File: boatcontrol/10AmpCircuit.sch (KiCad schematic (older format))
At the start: 5 parts, among them K6801 G5RL-K1A-E-DC12, Q6801 T9-818 10A, SW6801 ESB30, SW6802 ESB30

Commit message: Fix graphics
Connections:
- net ON_COIL: now reaches K6801.1 (C1), SW6801.2 (B), SW6801.5 (B)
- net TO_FUSE: now reaches K6801.4 (NO), K6801.5 (NO), Q6801.P1 (P?)
- net OFF_COIL: now reaches K6801.8 (C8), SW6802.2 (B), SW6802.5 (B)
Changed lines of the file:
@@
 $Descr A4 11693 8268
 encoding utf-8
-Sheet 67 87
+Sheet 76 87
 Title "Boat Control Hat"
 Date "2020-07-09"
@@
 Wire Wire Line
 	5250 4000 5250 4900
+Text Label 6750 3550 0    50   ~ 0
+ON_COIL
+Text Label 6700 4500 0    50   ~ 0
+OFF_COIL
+Text Label 7350 3650 0    50   ~ 0
+TO_FUSE
 $EndSCHEMATC

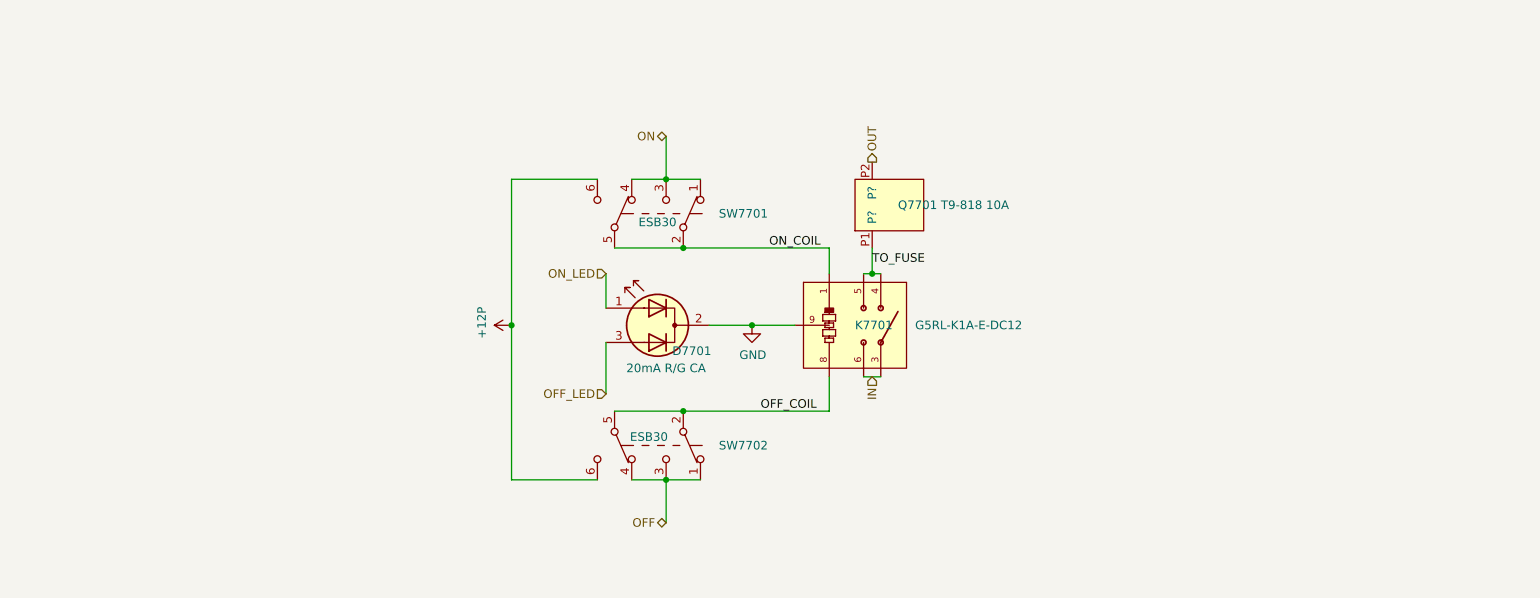
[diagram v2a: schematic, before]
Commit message: Fix switch layouts
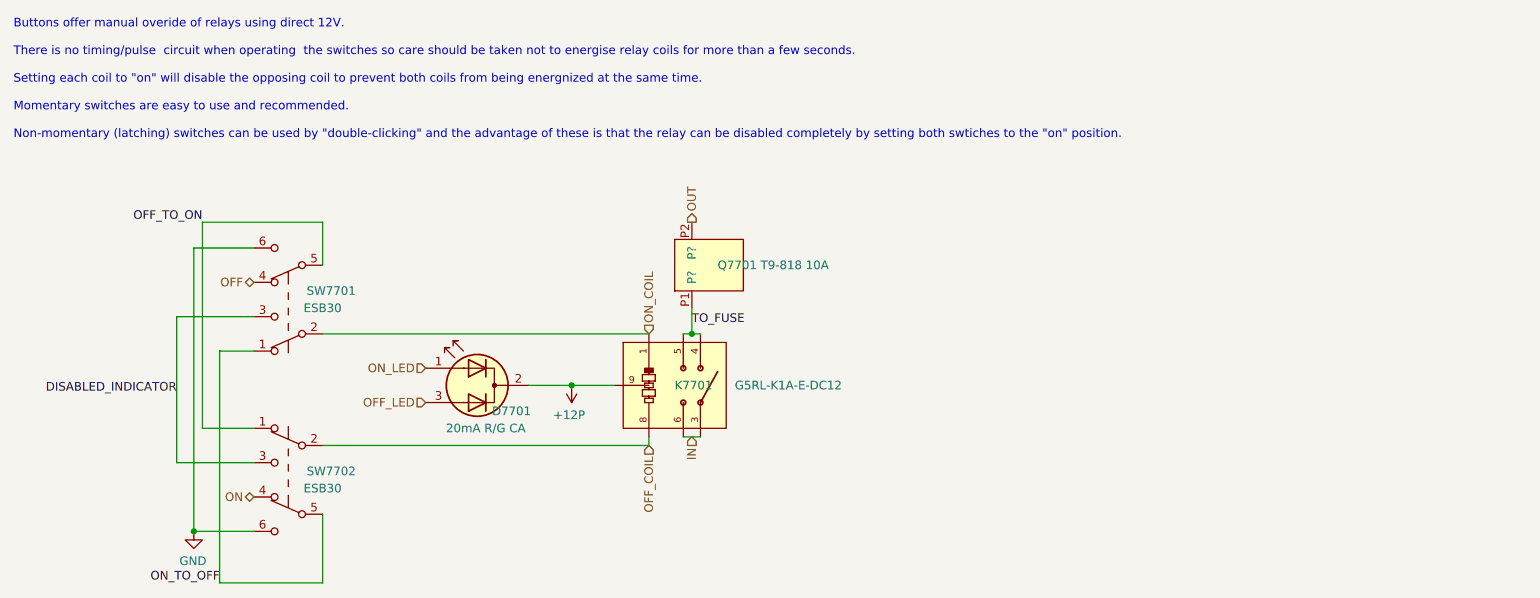
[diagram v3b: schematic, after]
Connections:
- net +12P: now also D6801.2 (K), K6801.9 (C9); no longer SW6801.6 (C), SW6802.6 (C)
- net GND: now also SW6801.6 (C), SW6802.6 (C); no longer D6801.2 (K), K6801.9 (C9)
- net OFF: now also SW6801.4 (A); no longer SW6802.1 (A), SW6802.3 (C), SW6802.4 (A)
- net OFF_COIL: no longer SW6802.5 (B)
- net ON: now also SW6802.4 (A); no longer SW6801.1 (A), SW6801.3 (C), SW6801.4 (A)
- net ON_COIL: no longer SW6801.5 (B)
- new net DISABLED_INDICATOR: SW6801.3 (C), SW6802.3 (C)
- new net OFF_TO_ON: SW6801.5 (B), SW6802.1 (A)
- new net ON_TO_OFF: SW6801.1 (A), SW6802.5 (B)
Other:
- note added: "Buttons offer manual overide of relays using direct 12V.\n\nThere is no timing/pulse circuit when operating the switches so care should be taken not to energise relay coils for more than a few seconds.\n\nSetting each coil to "on" will disable the opposing coil to prevent both coils from being energnized at the same time.\n\nMomentary switches are easy to use and recommended.\n\nNon-momentary (la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"
- moved on the sheet: D7701, K7701, Q7701, SW7701, SW7702

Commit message: Before re-order
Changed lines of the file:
@@
 $Descr A4 11693 8268
 encoding utf-8
-Sheet 77 87
+Sheet 67 87
 Title "Boat Control Hat"
 Date "2020-07-09"
@@
 AR Path="/D1BB8DB4/5F75E923/60474907/D2F4DB55" Ref="D7601"  Part="1"
 AR Path="/D1BB8DB4/5F75E923/60474911/D2F4DB55" Ref="D7701"  Part="1"
-F 0 "D7701" H 4850 4200 50  0000 C CNN
+F 0 "D6701" H 4850 4200 50  0000 C CNN
 F 1 "20mA R/G CA" H 5000 4100 50  0000 C CNN
 F 2 "LED_THT:LED_D5.0mm-3" H 5050 4350 50  0001 C CNN
@@
 AR Path="/D1BB8DB4/5F75E923/60474907/6123E07D" Ref="K7601"  Part="1"
 AR Path="/D1BB8DB4/5F75E923/60474911/6123E07D" Ref="K7701"  Part="1"
-F 0 "K7701" H 6200 4350 50  0000 L CNN
+F 0 "K6701" H 6200 4350 50  0000 L CNN
 F 1 "G5RL-K1A-E-DC12" H 6550 4350 50  0000 L CNN
 F 2 "RELAY_G5RL-K1A-E-DC12" H 6550 4500 50  0001 L BNN
@@
 AR Path="/D1BB8DB4/5F75E923/60474907/D2F4DB59" Ref="SW7601"  Part="1"
 AR Path="/D1BB8DB4/5F75E923/60474911/D2F4DB59" Ref="SW7701"  Part="1"
-F 0 "SW7701" H 3700 3800 50  0000 C CNN
+F 0 "SW6701" H 3700 3800 50  0000 C CNN
 F 1 " ESB30" H 3750 3900 50  0000 C CNN
 F 2 "BoatControl:SW_PUSH_ESB30_DPDT" H 3950 4050 50  0001 C CNN
@@
 AR Path="/D1BB8DB4/5F75E923/60474907/D2F4DB57" Ref="SW7602"  Part="1"
 AR Path="/D1BB8DB4/5F75E923/60474911/D2F4DB57" Ref="SW7702"  Part="1"
-F 0 "SW7702" H 3700 4950 50  0000 C CNN
+F 0 "SW6702" H 3700 4950 50  0000 C CNN
 F 1 " ESB30" H 3750 4850 50  0000 C CNN
 F 2 "BoatControl:SW_PUSH_ESB30_DPDT" H 3950 5100 50  0001 C CNN
@@
 AR Path="/D1BB8DB4/5F75E923/60474907/D2F4DB58" Ref="Q7601"  Part="1"
 AR Path="/D1BB8DB4/5F75E923/60474911/D2F4DB58" Ref="Q7701"  Part="1"
-F 0 "Q7701" V 6100 3300 50  0000 R CNN
+F 0 "Q6701" V 6100 3300 50  0000 R CNN
 F 1 "T9-818 10A" V 6100 3050 50  0000 R CNN
 F 2 "BoatControl:Schurter_Circuit_Breaker" H 6100 3650 50  0001 C CNN

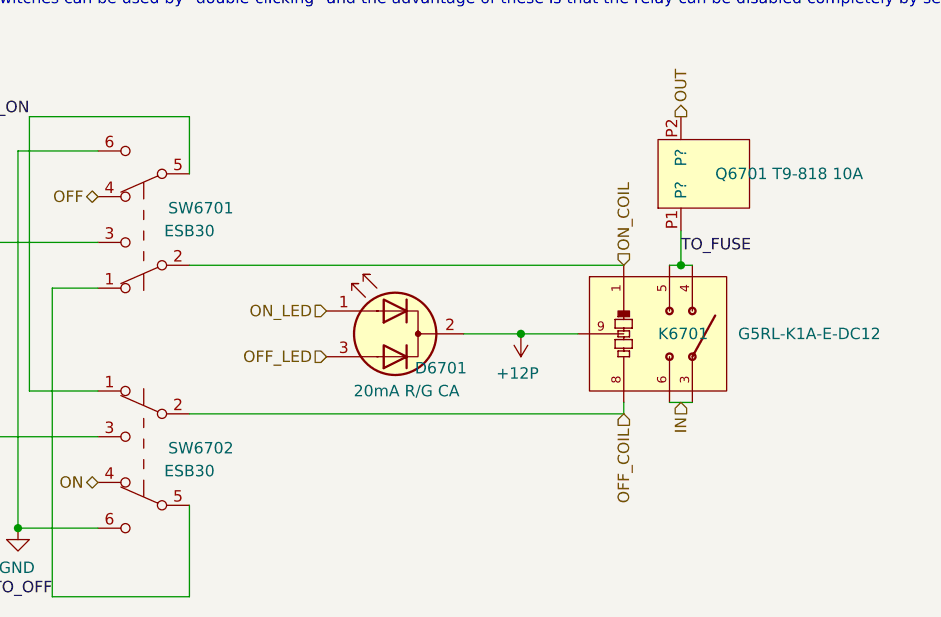
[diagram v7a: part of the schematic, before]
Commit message: Add remaining bypass capacitors
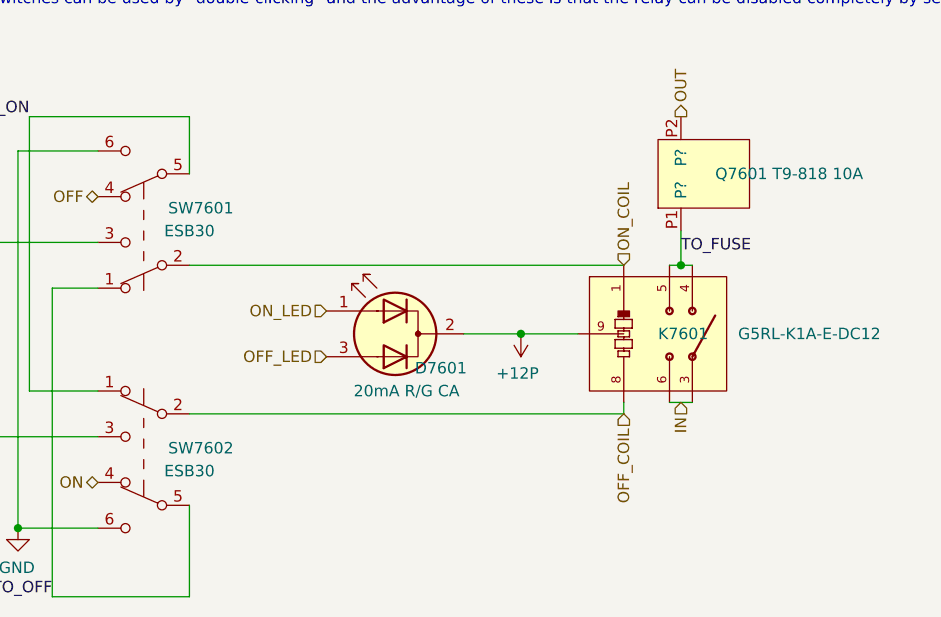
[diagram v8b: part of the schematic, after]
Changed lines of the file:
@@
 AR Path="/D1BB8DB4/5F75E923/60474907/D2F4DB55" Ref="D7601"  Part="1"
 AR Path="/D1BB8DB4/5F75E923/60474911/D2F4DB55" Ref="D7701"  Part="1"
-F 0 "D6701" H 4850 4200 50  0000 C CNN
+F 0 "D7601" H 4850 4200 50  0000 C CNN
 F 1 "20mA R/G CA" H 5000 4100 50  0000 C CNN
 F 2 "LED_THT:LED_D5.0mm-3" H 5050 4350 50  0001 C CNN
@@
 AR Path="/D1BB8DB4/5F75E923/60474907/6123E07D" Ref="K7601"  Part="1"
 AR Path="/D1BB8DB4/5F75E923/60474911/6123E07D" Ref="K7701"  Part="1"
-F 0 "K6701" H 6200 4350 50  0000 L CNN
+F 0 "K7601" H 6200 4350 50  0000 L CNN
 F 1 "G5RL-K1A-E-DC12" H 6550 4350 50  0000 L CNN
 F 2 "RELAY_G5RL-K1A-E-DC12" H 6550 4500 50  0001 L BNN
@@
 AR Path="/D1BB8DB4/5F75E923/60474907/D2F4DB59" Ref="SW7601"  Part="1"
 AR Path="/D1BB8DB4/5F75E923/60474911/D2F4DB59" Ref="SW7701"  Part="1"
-F 0 "SW6701" H 3700 3800 50  0000 C CNN
+F 0 "SW7601" H 3700 3800 50  0000 C CNN
 F 1 " ESB30" H 3750 3900 50  0000 C CNN
 F 2 "BoatControl:SW_PUSH_ESB30_DPDT" H 3950 4050 50  0001 C CNN
@@
 AR Path="/D1BB8DB4/5F75E923/60474907/D2F4DB57" Ref="SW7602"  Part="1"
 AR Path="/D1BB8DB4/5F75E923/60474911/D2F4DB57" Ref="SW7702"  Part="1"
-F 0 "SW6702" H 3700 4950 50  0000 C CNN
+F 0 "SW7602" H 3700 4950 50  0000 C CNN
 F 1 " ESB30" H 3750 4850 50  0000 C CNN
 F 2 "BoatControl:SW_PUSH_ESB30_DPDT" H 3950 5100 50  0001 C CNN
@@
 AR Path="/D1BB8DB4/5F75E923/60474907/D2F4DB58" Ref="Q7601"  Part="1"
 AR Path="/D1BB8DB4/5F75E923/60474911/D2F4DB58" Ref="Q7701"  Part="1"
-F 0 "Q6701" V 6100 3300 50  0000 R CNN
+F 0 "Q7601" V 6100 3300 50  0000 R CNN
 F 1 "T9-818 10A" V 6100 3050 50  0000 R CNN
 F 2 "BoatControl:Schurter_Circuit_Breaker" H 6100 3650 50  0001 C CNN
